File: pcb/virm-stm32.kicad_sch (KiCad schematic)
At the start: 0 parts

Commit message: Initial version
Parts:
- added U1: STM32F070F6Px, Package_SO:TSSOP-20_4.4x6.5mm_P0.65mm, symbol MCU_ST_STM32F0:STM32F070F6Px
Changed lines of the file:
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@@
 		(date "2024-03-10")
+	)
+	(symbol
+		(lib_id "MCU_ST_STM32F0:STM32F070F6Px")
+		(at 63.5 91.44 0)
+		(unit 1)
+		(exclude_from_sim no)
+		(in_bom yes)
+		(on_board yes)
+		(dnp no)
+		(fields_autoplaced yes)
+		(property "Reference" "U1"
+			(at 65.6941 111.76 0)
+			(effects
+				(font
+					(size 1.27 1.27)
+				)
+				(justify left)
+			)
+		)
+		(property "Value" "STM32F070F6Px"
+			(at 65.6941 114.3 0)
+			(effects
+				(font
+					(size 1.27 1.27)
+				)
+				(justify left)
+			)
+		)
+		(property "Footprint" "Package_SO:TSSOP-20_4.4x6.5mm_P0.65mm"
+			(at 50.8 109.22 0)
+			(effects
+				(font
+					(size 1.27 1.27)
+				)
+				(justify right)
+				(hide yes)
+			)
+		)
+		(property "Datasheet" "https://www.st.com/resource/en/datasheet/stm32f070f6.pdf"
+			(at 63.5 91.44 0)
+			(effects
+				(font
+					(size 1.27 1.27)
+				)
+				(hide yes)
+			)
+		)
+		(property "Description" "STMicroelectronics Arm Cortex-M0 MCU, 32KB flash, 6KB RAM, 48 MHz, 2.4-3.6V, 15 GPIO, TSSOP20"
+			(at 63.5 91.44 0)
+			(effects
+				(font
+					(size 1.27 1.27)
+				)
+				(hide yes)
+			)
+		)
+		(pin "20"
+		)
+		(pin "2"
+		)
+		(pin "18"
+		)
+		(pin "17"
+		)
+		(pin "19"
+		)
+		(pin "1"
+		)
+		(pin "15"
+		)
+		(pin "14"
+		)
+		(pin "13"
+		)
+		(pin "12"
+		)
+		(pin "11"
+		)
+		(pin "10"
+		)
+		(pin "16"
+		)
+		(pin "7"
+		)
+		(pin "4"
+		)
+		(pin "3"
+		)
+		(pin "5"
+		)
+		(pin "6"
+		)
+		(pin "8"
+		)
+		(pin "9"
+		)
+		(instances
+			(project "virm-stm32"
+				(path "/b59a39ad-0da4-44fb-8a67-225b8918cd11"
+					(reference "U1")
+					(unit 1)
+				)
+			)
+		)
 	)
 	(sheet_instances

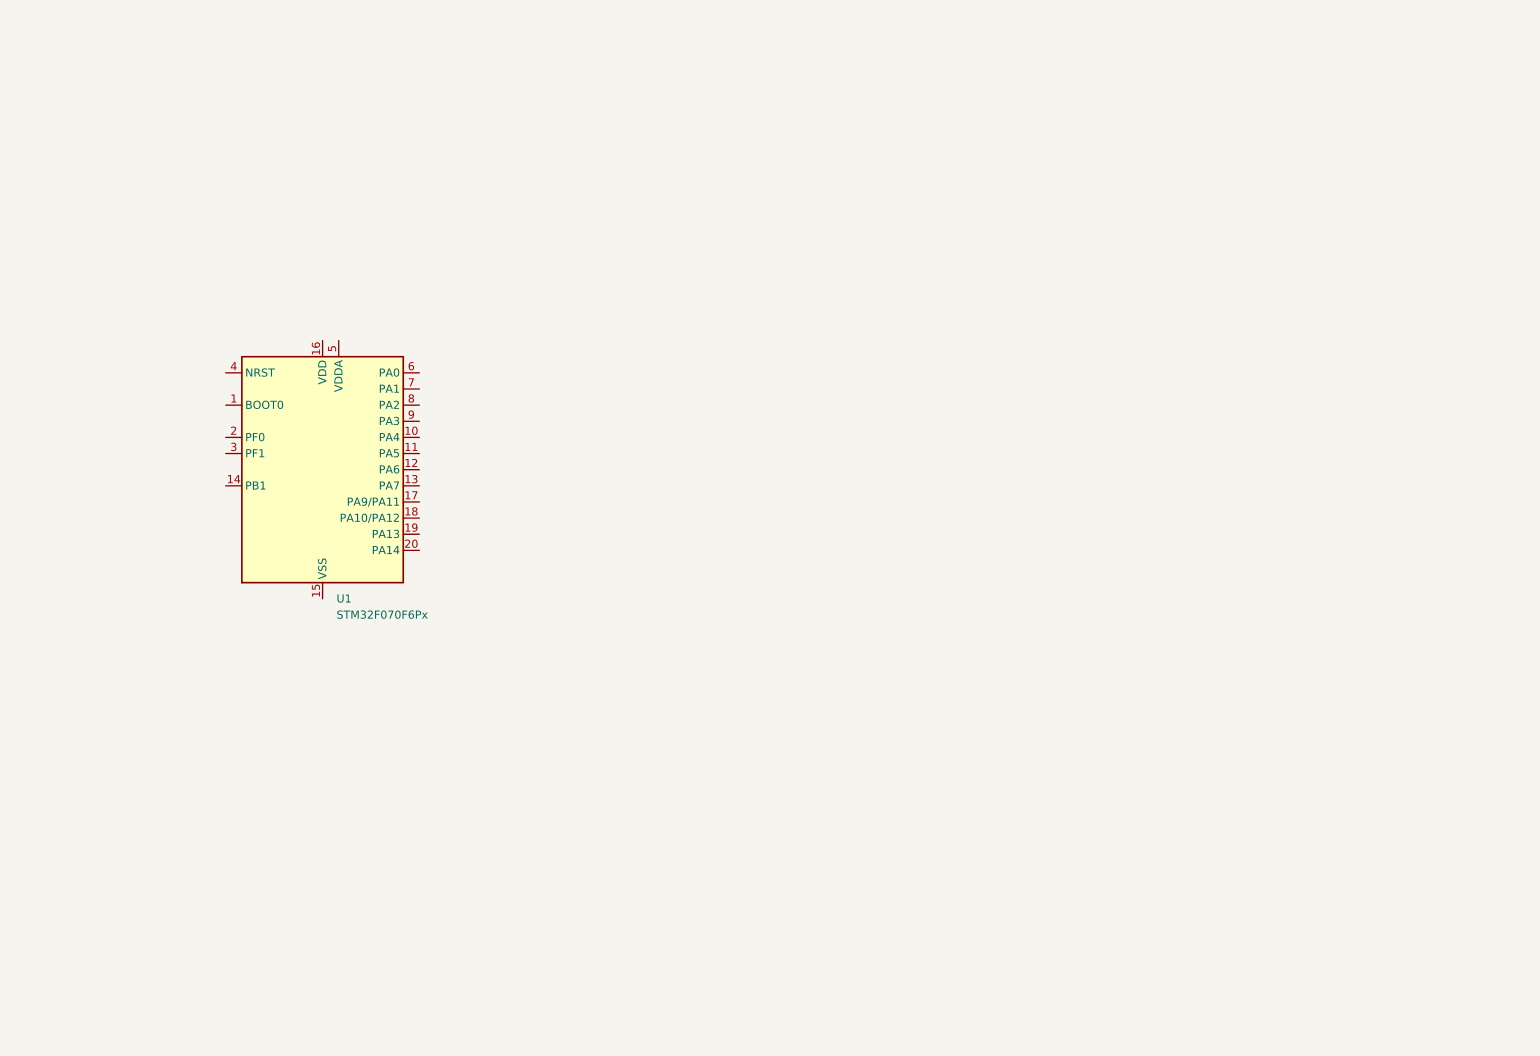
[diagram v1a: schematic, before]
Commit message: Added a power circuit
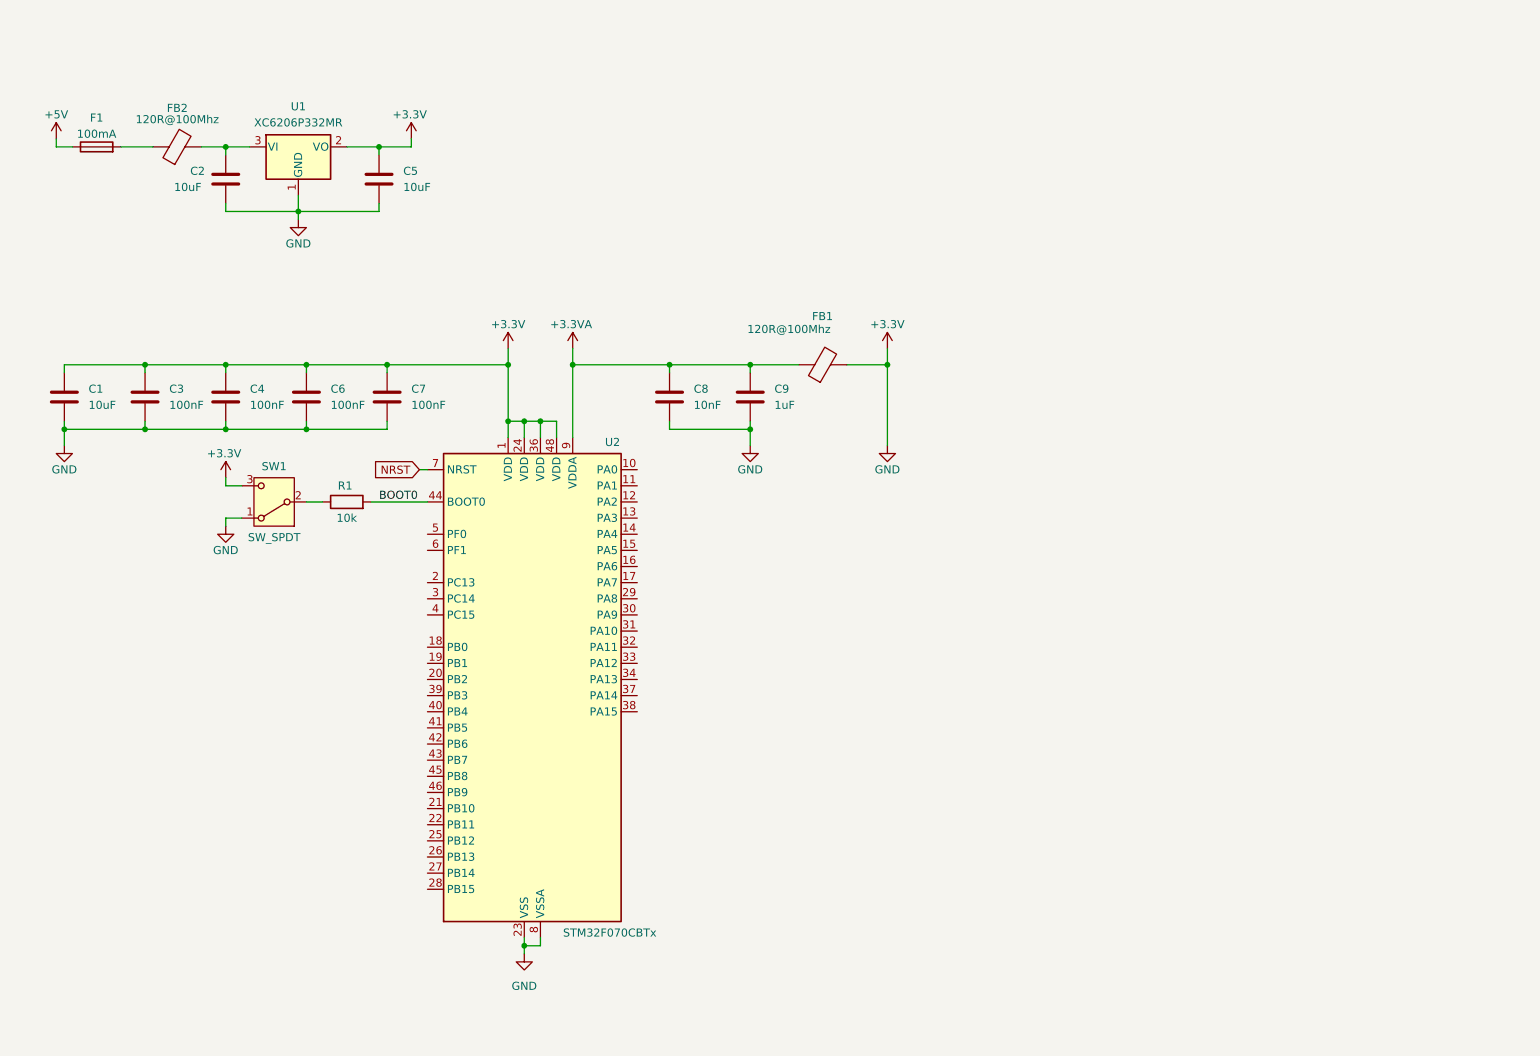
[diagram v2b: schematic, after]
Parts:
- removed U1: STM32F070F6Px, Package_SO:TSSOP-20_4.4x6.5mm_P0.65mm, symbol MCU_ST_STM32F0:STM32F070F6Px
- added C1, C2, C5: 10uF, symbol Device:C
- added C3, C4, C6, C7: 100nF, symbol Device:C
- added C8: 10nF, symbol Device:C
- added C9: 1uF, symbol Device:C
- added F1: 100mA, symbol Device:Fuse
- added FB1, FB2: 120R@100Mhz, symbol Device:FerriteBead
- added R1: 10k, symbol Device:R
- added SW1: SW_SPDT, symbol Switch:SW_SPDT
- added U1: XC6206P332MR, Package_TO_SOT_SMD:SOT-23-3, symbol Regulator_Linear:XC6206PxxxMR
- added U2: STM32F070CBTx, Package_QFP:LQFP-48_7x7mm_P0.5mm, symbol MCU_ST_STM32F0:STM32F070CBTx
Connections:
- new net: C2.1, FB2.2, U1.3 (VI)
- new net: F1.2, FB2.1
- new net: R1.1, SW1.2 (B)
- new net +3.3V: C1.1, C1.2, C2.2, C3.1, C3.2, C4.1, C4.2, C5.1, C5.2, C6.1, C6.2, C7.1, C7.2, C8.2, C9.2, FB1.2, SW1.1 (A), SW1.3 (C), U1.1 (GND), U1.2 (VO), U2.1 (VDD), U2.23 (VSS), U2.24 (VDD), U2.35 (VSS), U2.36 (VDD), U2.47 (VSS), U2.48 (VDD), U2.8 (VSSA)
- new net +3.3VA: C8.1, C9.1, FB1.1, U2.9 (VDDA)
- new net +5V: F1.1
- new net BOOT0: R1.2, U2.44 (BOOT0)
- new net NRST: U2.7 (NRST)
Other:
- company: (none) -> Martijn Casteel
- title: VIRM STM32 -> VIRM-STM32

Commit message: Added a led matrix using charlieplexing
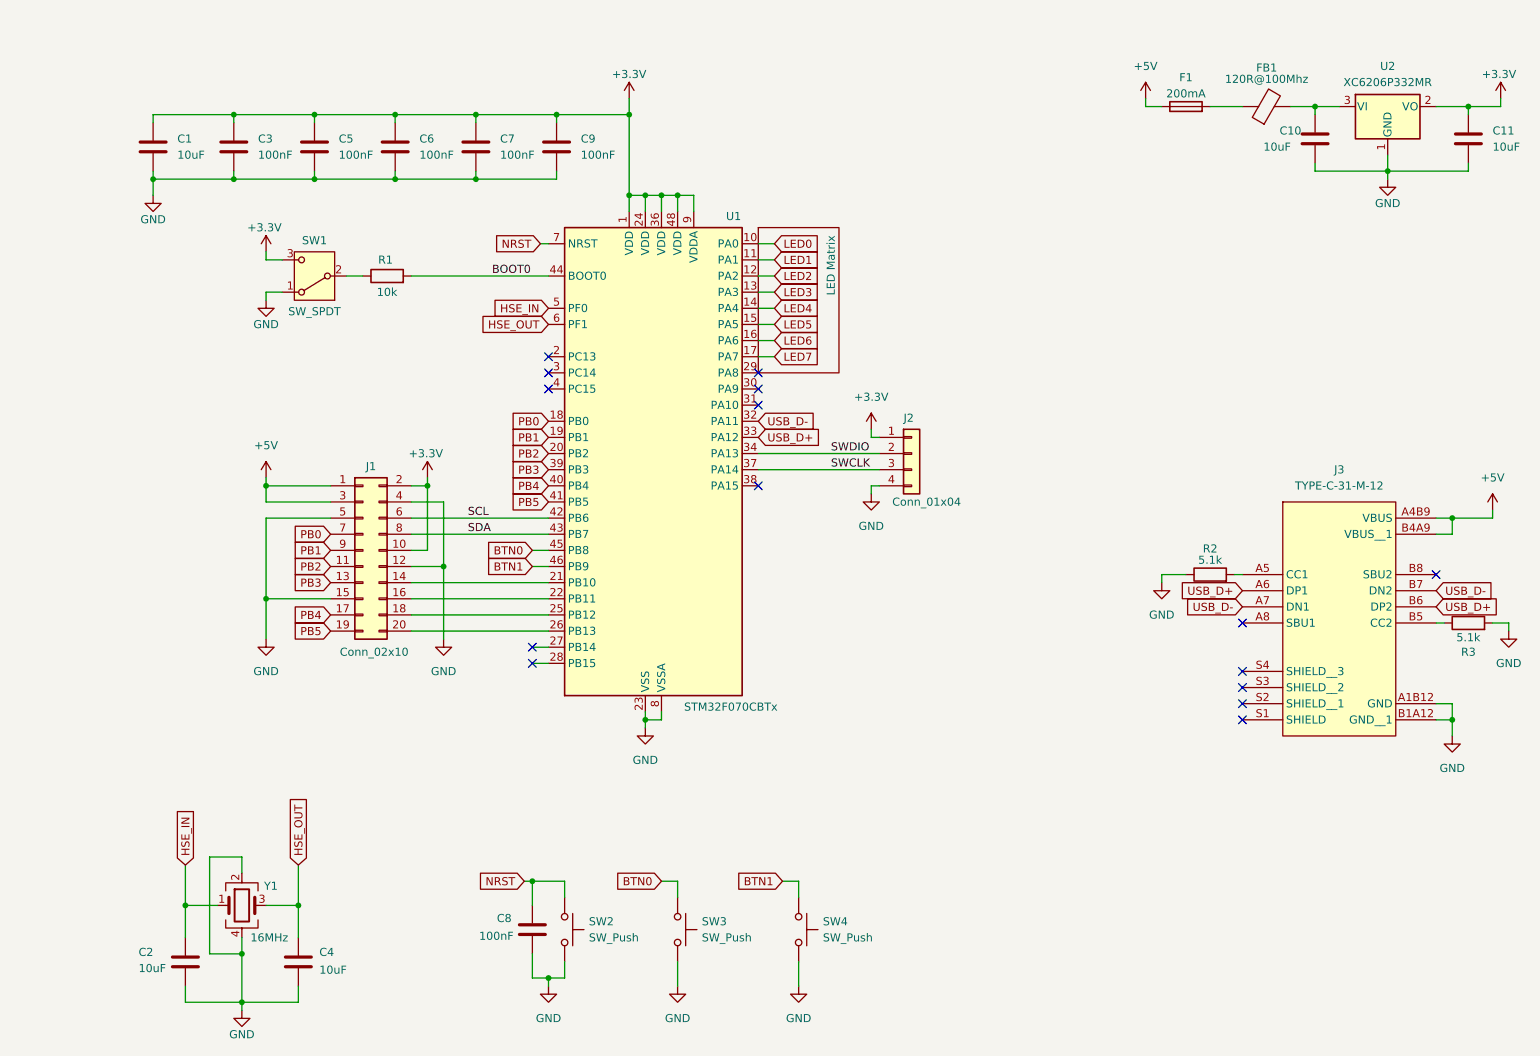
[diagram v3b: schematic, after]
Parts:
- removed FB1: 120R@100Mhz, symbol Device:FerriteBead
- added C2, C4: 10uF, symbol Device:C
- added J1: Conn_02x10, symbol Connector_Generic:Conn_02x10_Odd_Even
- added J2: Conn_01x04, symbol Connector_Generic:Conn_01x04
- added J3: TYPE-C-31-M-12, symbol LCSC:TYPE-C-31-M-12
- added R2, R3: 5.1k, symbol Device:R
- added SW2, SW3, SW4: SW_Push, symbol Switch:SW_Push
- added Y1: 16MHz, symbol Device:Crystal_GND24
- C8: value 10nF -> 100nF
- C9: value 1uF -> 100nF
- F1: value 100mA -> 200mA
- U1: renamed from U2; LCSC (none) -> C74909
- U2: renamed from U1; LCSC (none) -> C5446
- renumbered C2 to C10, C5 to C11, C4 to C5, FB2 to FB1
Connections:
- net +3.3V: now also C9.1, U1.9 (VDDA), J1.10 (Pin_10), J1.2 (Pin_2), J2.1 (Pin_1); no longer C1.2, C10.2, C11.2, C3.2, C5.2, C6.2, C7.2, C8.2, C9.2, SW1.1 (A), U1.23 (VSS), U1.35 (VSS), U1.47 (VSS), U1.8 (VSSA), U2.1 (GND)
- net +5V: now also J1.1 (Pin_1), J1.3 (Pin_3), J3.A4B9 (VBUS), J3.B4A9 (VBUS__1)
- net NRST: now also C8.1, SW2.1
- net LED0: now reaches U1.10 (PA0)
- net LED1: now reaches U1.11 (PA1)
- net LED2: now reaches U1.12 (PA2)
- net LED3: now reaches U1.13 (PA3)
- net LED4: now reaches U1.14 (PA4)
- net LED5: now reaches U1.15 (PA5)
- net LED6: now reaches U1.16 (PA6)
- net LED7: now reaches U1.17 (PA7)
- net PB0: now reaches U1.18 (PB0)
- net PB0: now also J1.7 (Pin_7)
- net PB1: now reaches U1.19 (PB1)
- net PB1: now also J1.9 (Pin_9)
- net PB2: now reaches U1.20 (PB2)
- net PB2: now also J1.11 (Pin_11)
- net at U1.21 (PB10): now also J1.14 (Pin_14)
- net at U1.22 (PB11): now also J1.16 (Pin_16)
- net at U1.25 (PB12): now also J1.18 (Pin_18)
- net at U1.26 (PB13): now also J1.20 (Pin_20)
- net USB_D-: now reaches U1.32 (PA11)
- net USB_D-: now also J3.A7 (DN1), J3.B7 (DN2)
- net USB_D+: now reaches U1.33 (PA12)
- net USB_D+: now also J3.A6 (DP1), J3.B6 (DP2)
- net SWDIO: now reaches U1.34 (PA13)
- net SWDIO: now also J2.2 (Pin_2)
- net SWCLK: now reaches U1.37 (PA14)
- net SWCLK: now also J2.3 (Pin_3)
- net PB3: now reaches U1.39 (PB3)
- net PB3: now also J1.13 (Pin_13)
- net PB4: now reaches U1.40 (PB4)
- net PB4: now also J1.17 (Pin_17)
- net PB5: now reaches U1.41 (PB5)
- net PB5: now also J1.19 (Pin_19)
- net SCL: now reaches U1.42 (PB6)
- net SCL: now also J1.6 (Pin_6)
- net SDA: now reaches U1.43 (PB7)
- net SDA: now also J1.8 (Pin_8)
- net BTN0: now reaches U1.45 (PB8)
- net BTN0: now also SW3.1
- net BTN1: now reaches U1.46 (PB9)
- net BTN1: now also SW4.1
- net HSE_IN: now reaches U1.5 (PF0)
- net HSE_IN: now also C2.1, Y1.1
- net HSE_OUT: now reaches U1.6 (PF1)
- net HSE_OUT: now also C4.1, Y1.3
- removed net +3.3VA: C8.1, C9.1, U1.9 (VDDA)
- new net: J3.A5 (CC1), R2.2
- new net: J3.B5 (CC2), R3.1
- new net GND: C1.2, C10.2, C11.2, C2.2, C3.2, C4.2, C5.2, C6.2, C7.2, C8.2, C9.2, J1.12 (Pin_12), J1.15 (Pin_15), J1.4 (Pin_4), J1.5 (Pin_5), J2.4 (Pin_4), J3.A1B12 (GND), J3.B1A12 (GND__1), R2.1, R3.2, SW1.1 (A), SW2.2, SW3.2, SW4.2, U1.23 (VSS), U1.35 (VSS), U1.47 (VSS), U1.8 (VSSA), U2.1 (GND), Y1.2, Y1.4
- no-connect marks 0 -> 15
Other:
- added sheet LED Matrix (led-matrix.kicad_sch)
- moved on the sheet: C1, C10, C11, C3, C5, C6, C7, F1, FB1, R1, SW1, U1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

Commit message: Added footprints, except for the USB port
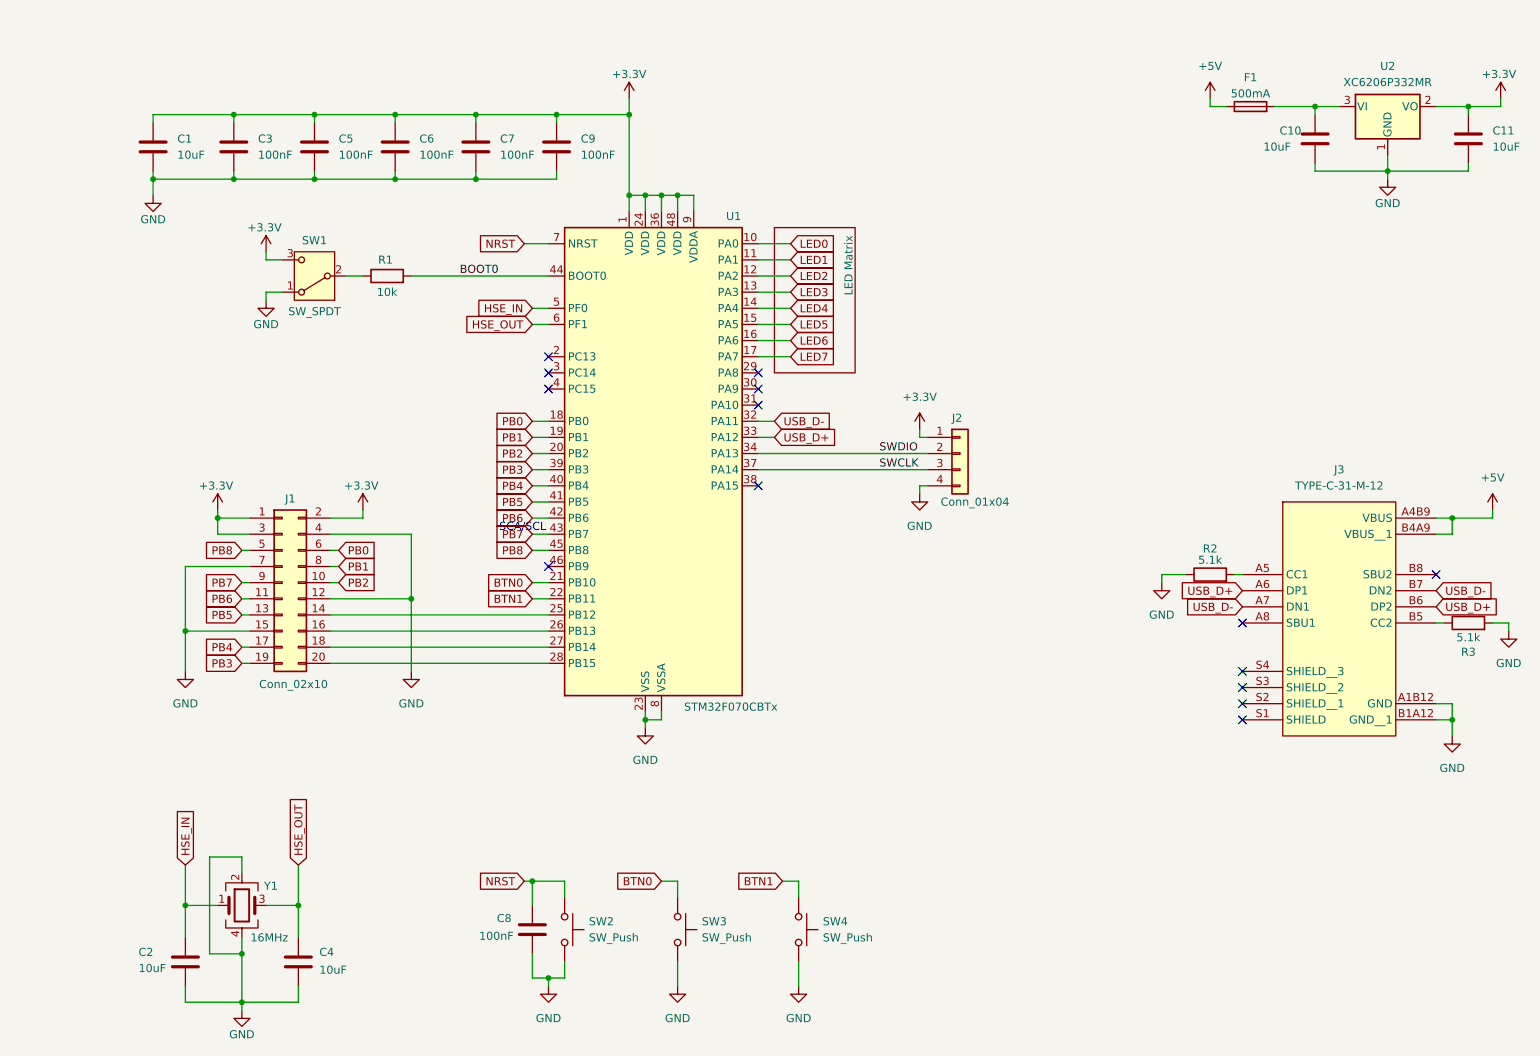
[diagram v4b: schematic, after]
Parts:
- removed FB1: 120R@100Mhz, symbol Device:FerriteBead
- C1, C10, C11, C2, C4: footprint (none) -> Capacitor_SMD:C_0402_1005Metric; lcsc (none) -> C15525
- C3, C5, C6, C7, C8, C9: footprint (none) -> Capacitor_SMD:C_0402_1005Metric; lcsc (none) -> C1525
- F1: value 200mA -> 500mA; footprint (none) -> Fuse:Fuse_0603_1608Metric; lcsc (none) -> C261937
- J1: footprint (none) -> Connector_PinHeader_2.54mm:PinHeader_2x10_P2.54mm_Vertical
- J2: footprint (none) -> Connector_PinSocket_2.54mm:PinSocket_1x04_P2.54mm_Vertical
- J3: lcsc (none) -> C165948
- R1: footprint (none) -> Resistor_SMD:R_0603_1608Metric; lcsc (none) -> C25804
- R2, R3: footprint (none) -> Resistor_SMD:R_0603_1608Metric; lcsc (none) -> C23186
- SW1: footprint (none) -> Button_Switch_SMD:SW_SPDT_PCM12; lcsc (none) -> C778186
- SW2, SW3, SW4: footprint (none) -> Button_Switch_SMD:SW_Push_1P1T_XKB_TS-1187A
- U1: LCSC C74909 -> (none); lcsc (none) -> C74909
- U2: LCSC C5446 -> (none); lcsc (none) -> C5446
- Y1: footprint (none) -> Crystal:Crystal_SMD_3225-4Pin_3.2x2.5mm; LCSC C112972 -> (none); lcsc (none) -> C112972
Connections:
- net +3.3V: now also J1.1 (Pin_1), J1.3 (Pin_3); no longer J1.10 (Pin_10)
- net +5V: no longer J1.1 (Pin_1), J1.3 (Pin_3)
- net BTN0: now also U1.21 (PB10); no longer U1.45 (PB8)
- net BTN1: now also U1.22 (PB11); no longer U1.46 (PB9)
- net GND: now also J1.7 (Pin_7); no longer J1.5 (Pin_5)
- net PB0: now also J1.6 (Pin_6); no longer J1.7 (Pin_7)
- net PB1: now also J1.8 (Pin_8); no longer J1.9 (Pin_9)
- net PB2: now also J1.10 (Pin_10); no longer J1.11 (Pin_11)
- net PB3: now also J1.19 (Pin_19); no longer J1.13 (Pin_13)
- net PB5: now also J1.13 (Pin_13); no longer J1.19 (Pin_19)
- net at C10.1, U2.3 (VI): now also F1.2
- net at J1.14 (Pin_14): now also U1.25 (PB12); no longer U1.21 (PB10)
- net at J1.16 (Pin_16): now also U1.26 (PB13); no longer U1.22 (PB11)
- net at J1.18 (Pin_18): now also U1.27 (PB14); no longer U1.25 (PB12)
- net at J1.20 (Pin_20): now also U1.28 (PB15); no longer U1.26 (PB13)
- net SCL renamed PB6
- net PB6: now also J1.11 (Pin_11); no longer J1.6 (Pin_6)
- net SDA renamed PB7
- net PB7: now also J1.9 (Pin_9); no longer J1.8 (Pin_8)
- new net PB8: J1.5 (Pin_5), U1.45 (PB8)
- no-connect marks 15 -> 14
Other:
- note added: "SCA/SCL"
- moved on the sheet: F1, J1, J2
